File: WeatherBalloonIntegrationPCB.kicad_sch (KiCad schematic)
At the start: 11 parts, among them U1 ESP-32S

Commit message: Adding some stuff
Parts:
- added C1, C2: 100n, symbol Device:C
- added C3, C4: 22u, symbol Device:C_Polarized_US
- added U3: AMS1117-3.3, Package_TO_SOT_SMD:SOT-223-3_TabPin2, symbol Regulator_Linear:AMS1117-3.3
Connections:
- net +3.3V: now also C1.1, C3.1, U3.2 (VO)
- net GND: now also BT1.2 (-), U1.14 (GND1), U1.32 (GND2), U1.38 (GND3), U2.1 (GND), C1.2, C2.2, C3.2, C4.2, U3.1 (GND)
- net +BATT: now reaches BT1.1 (+)
- net +BATT: now also A1.8 (VIN), C2.1, C4.1, U3.3 (VI)
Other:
- moved on the sheet: A2, BT1

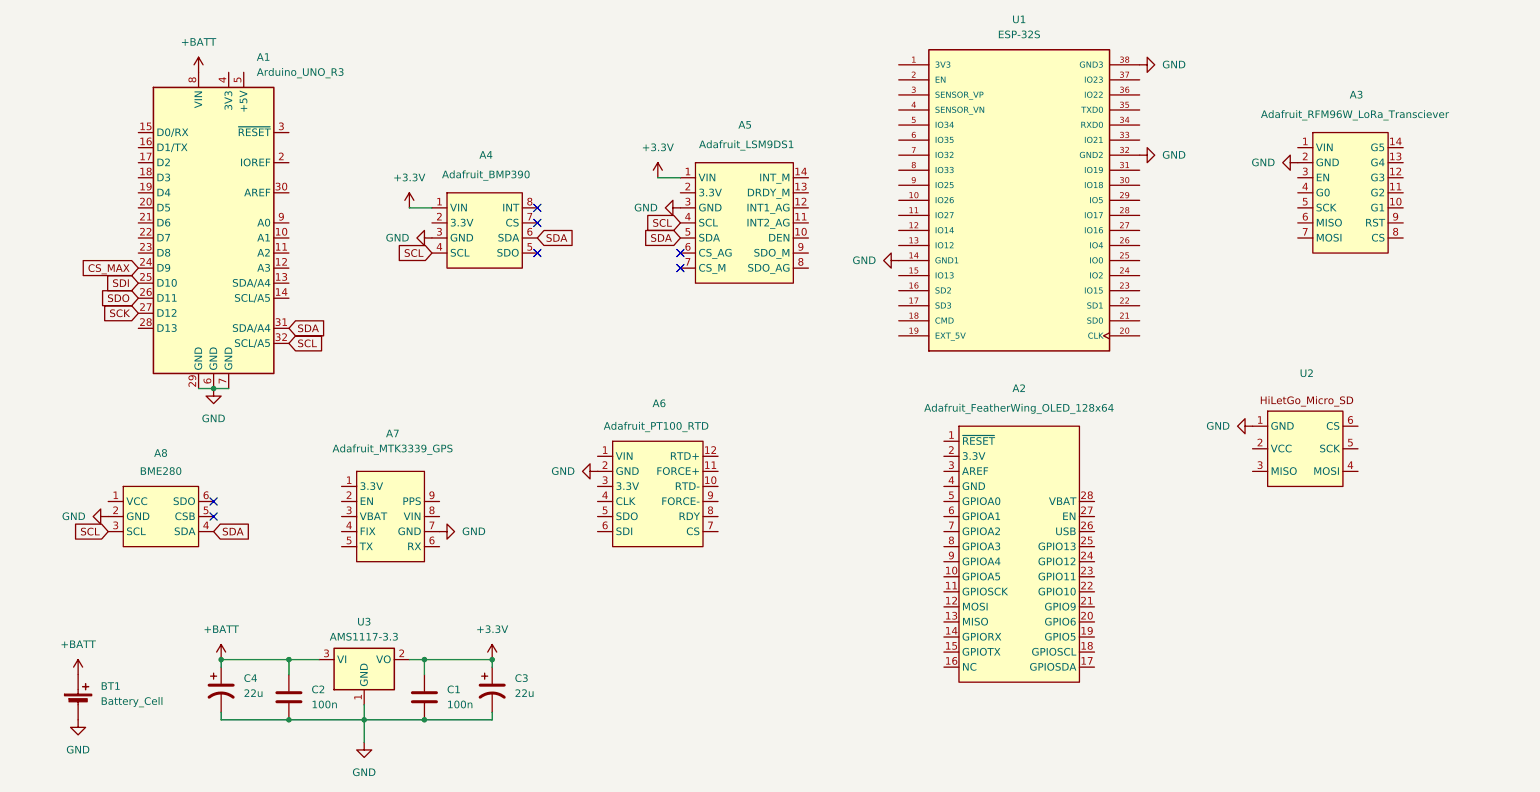
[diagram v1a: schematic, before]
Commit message: Connected most sensors
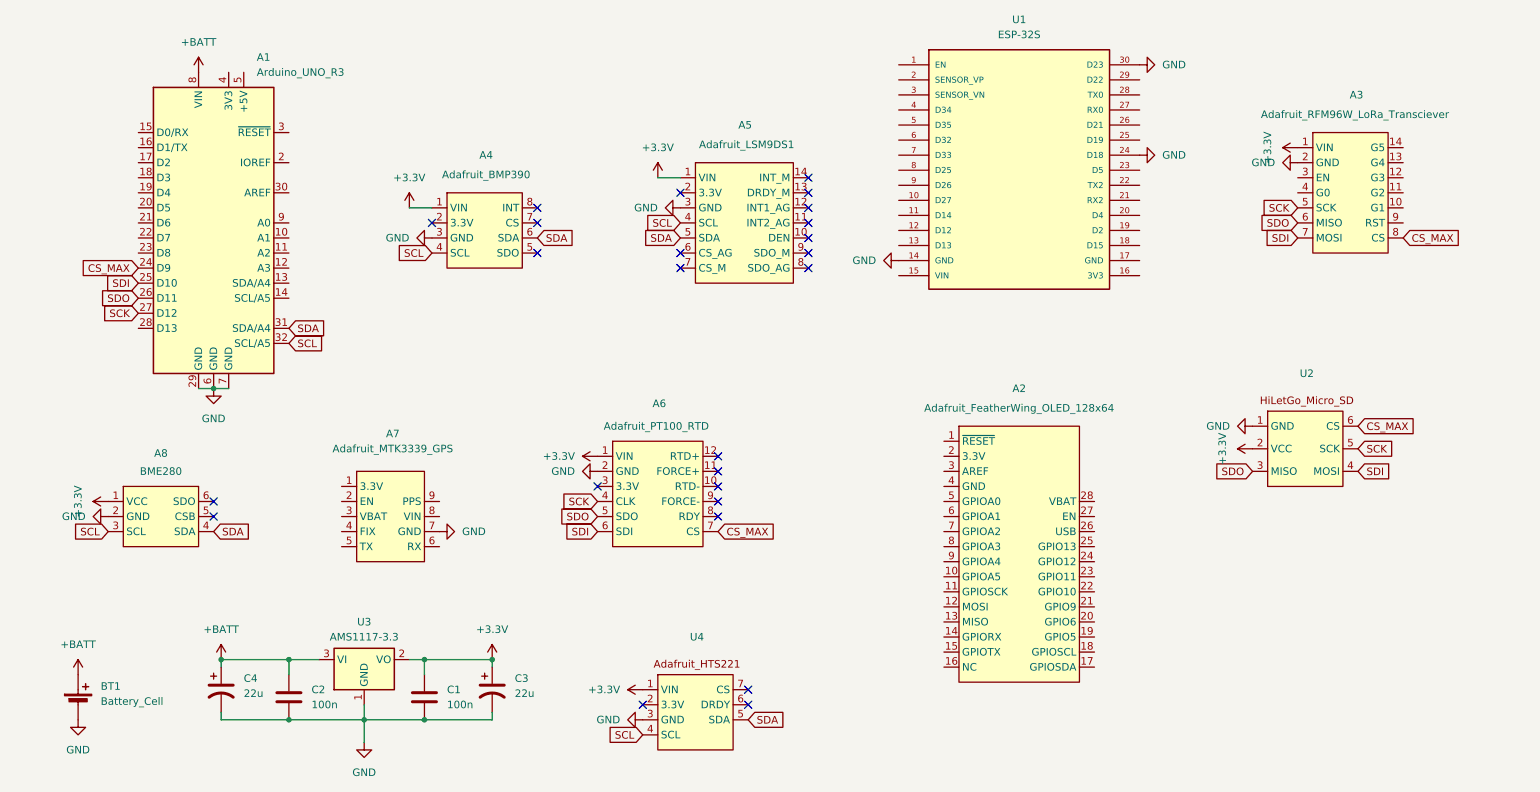
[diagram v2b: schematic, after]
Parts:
- added U4: ~, symbol TSL_Symbols:HTS221
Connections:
- net +3.3V: now also A3.1 (VIN), A6.1 (VIN), A8.1 (VCC), U2.2 (VCC), U4.1 (VIN)
- net CS_MAX: now also A3.8 (CS), A6.7 (CS), U2.6 (CS)
- net GND: now also U1.24 (D18), U1.30 (D23), U4.3 (GND); no longer U1.32 (GND2), U1.38 (GND3)
- net SCK: now also A3.5 (SCK), A6.4 (CLK), U2.5 (SCK)
- net SCL: now also U4.4 (SCL)
- net SDA: now also U4.5 (SDA)
- net SDI: now also A3.7 (MOSI), A6.6 (SDI), U2.4 (MOSI)
- net SDO: now also A3.6 (MISO), A6.5 (SDO), U2.3 (MISO)
- no-connect marks 7 -> 25

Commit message: some more connections
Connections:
- net CS_MAX: now also U1.13 (D13); no longer U2.6 (CS)
- net GND: now also U1.17 (GND); no longer U1.24 (D18), U1.30 (D23)
- net SCK: now also U1.24 (D18)
- net SCL: now also U1.29 (D22)
- net SDA: now also U1.26 (D21)
- net SDI: now also U1.30 (D23)
- net SDO: now also U1.25 (D19)
- net CS_SDCARD: now reaches A1.23 (D8)
- net CS_SDCARD: now also U1.18 (D15), U2.6 (CS)

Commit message: Connections
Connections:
- net +3.3V: now also A2.2 (3.3V), A7.8 (VIN), U1.15 (VIN)
- net CS_MAX: no longer A3.8 (CS)
- net GND: now also A2.4 (GND)
- net SCL: now also A2.18 (GPIOSCL)
- net SDA: now also A2.17 (GPIOSDA)
- net IQR_Transciever: now reaches A3.4 (G0)
- net IQR_Transciever: now also A1.18 (D3), U1.4 (D34)
- net RST_Transciever: now reaches A3.9 (RST)
- net RST_Transciever: now also A1.19 (D4), U1.5 (D35)
- net GPS_TX: now reaches A7.5 (TX)
- net GPS_TX: now also A1.15 (D0/RX), U1.27 (RX0)
- net GPS_RX: now reaches A7.6 (RX)
- net GPS_RX: now also A1.16 (D1/TX), U1.28 (TX0)
- net RST_Display: now reaches A1.20 (D5)
- net RST_Display: now also A2.1 (~{RESET}), U1.6 (D32)
- net CS_Transciever: now reaches A1.21 (D6)
- net CS_Transciever: now also A3.8 (CS), U1.7 (D33)
- no-connect marks 25 -> 85
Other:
- moved on the sheet: A5
